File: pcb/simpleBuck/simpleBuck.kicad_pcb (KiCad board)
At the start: 4 copper layers, 76.2 x 50.8 mm, 65 parts, among them J1 Conn_01x04, J2 Conn_01x06, J3 Conn_01x04, J4 Conn_01x02, J5 Conn_01x02, J6 Conn_01x02, Q1 TRANSISTOR_PNPMMBT4403, U1 TI_INA181A2, U2 TI_TL072HIDBVR, U3 TI_TL072HIDBVR, U4 NATIONALSEMI_LM2596SX-ADJ, U5 ANALOG_MAX539BCSA+, U6 ANALOG_MAX539BCSA+

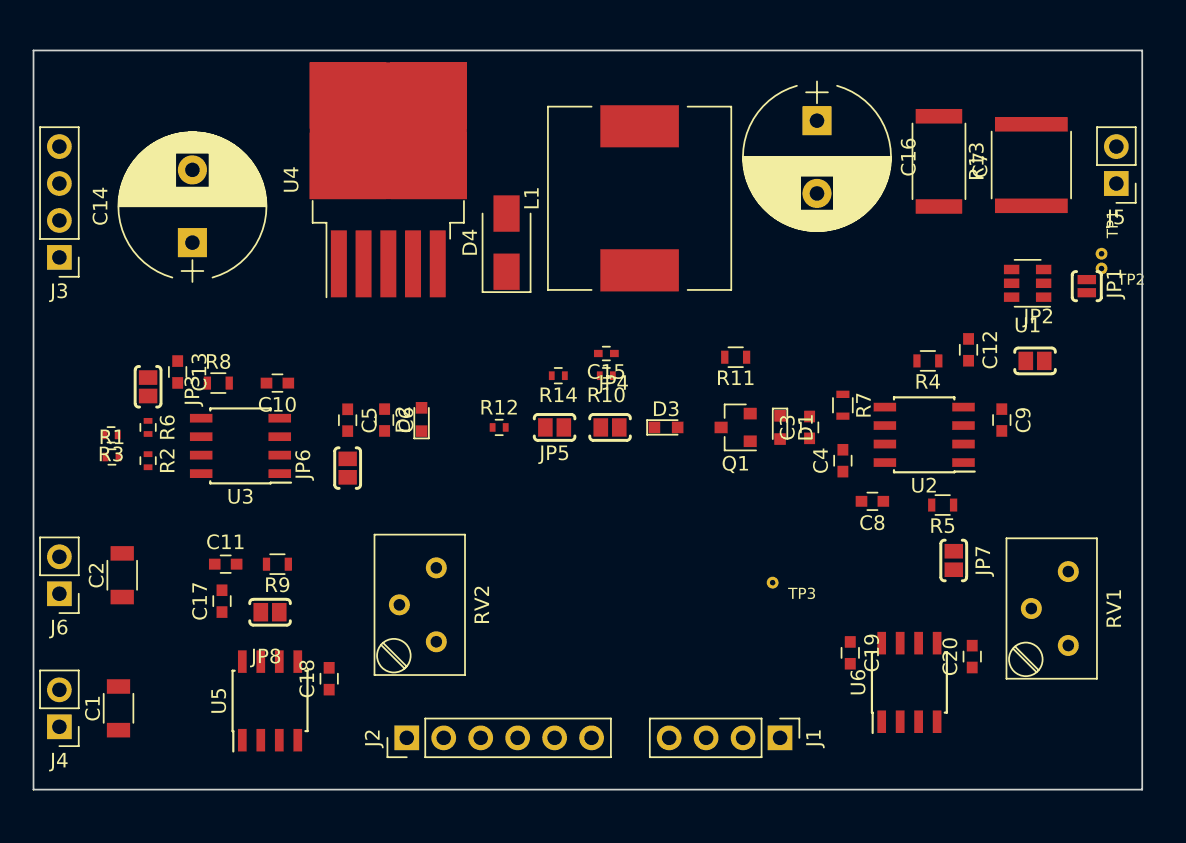
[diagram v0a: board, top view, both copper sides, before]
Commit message: Updated schematic to include lm2596 on board.
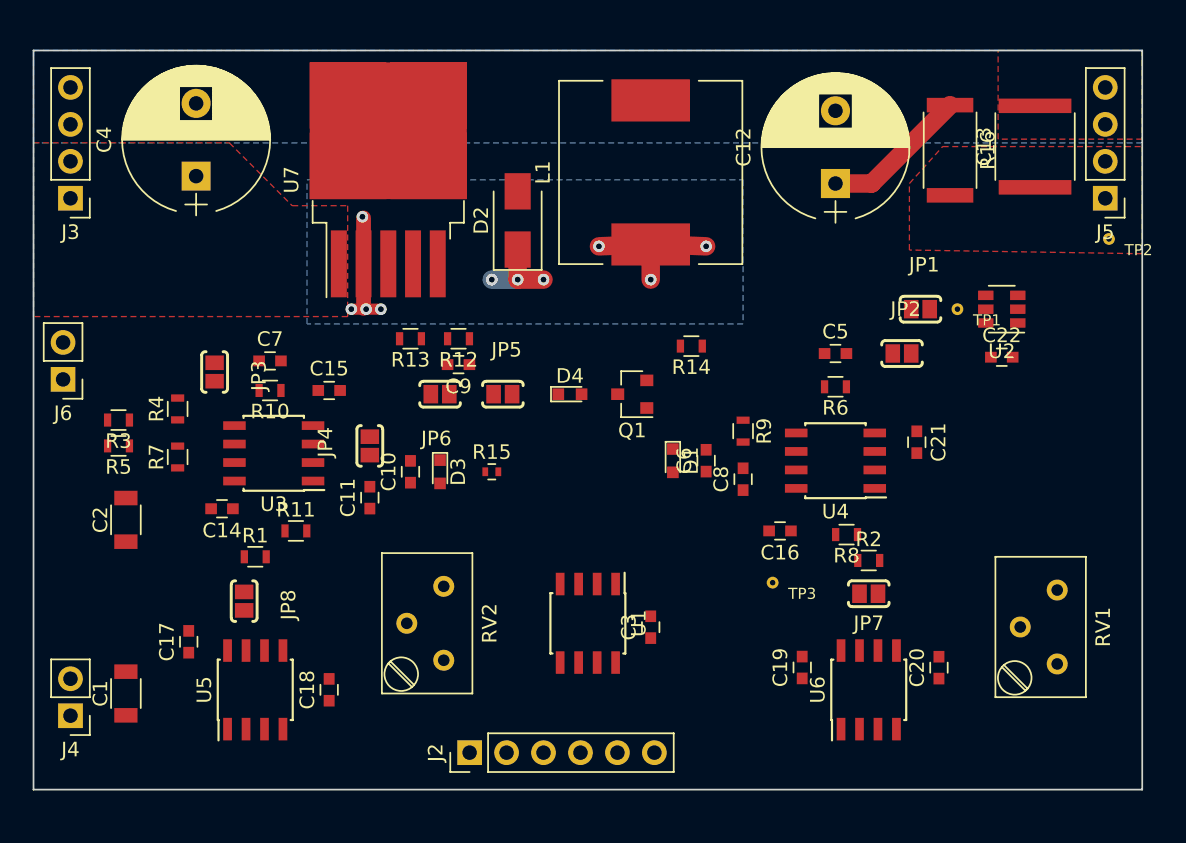
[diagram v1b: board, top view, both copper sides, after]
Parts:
- removed J1: Conn_01x04, Pin_Headers:Pin_Header_Straight_1x04_Pitch2.54mm
- added C21: MURATA_GCJ188R91H104KA01D, Capacitors_SMD:C_0603, F.Cu at (975.1, 204.7)
- added C22: MURATA_GCJ188R91H104KA01D, Capacitors_SMD:C_0603, F.Cu at (980.9, 198.9)
- added R15: VISHAYDALE_CRCW0402150KFKEDC, Resistors_SMD:R_0402, F.Cu at (945.9, 206.8)
- added R16: STACKPOLE_CSRT2512FT50L0-UP, Resistors_SMD:R_2512, F.Cu at (977.4, 184.7)
- added U7: NATIONALSEMI_LM2596SX-ADJ, TO_SOT_Packages_SMD:TO-263-5_TabPin6, F.Cu at (938.8, 186.7)
- C10, C11, C8, C9: value MURATA_GCJ188R91H104KA01D -> KEMET_C0603C103K5RAL7867
- C12: value KEMET_C0603C103K5RAL7867 -> PANASONIC_EEU-FC1H221B; footprint Capacitors_SMD:C_0603 -> Capacitors_THT:CP_Radial_D10.0mm_P5.00mm
- C13: value KEMET_C0603C103K5RAL7867 -> MURATA_KRM55WR7YA476MH01L; footprint Capacitors_SMD:C_0603 -> Capacitors_SMD:C_2220
- C14: value RUBYCON_100ZLH100MEFC10X20 -> MURATA_GCJ188R91H104KA01D; footprint Capacitors_THT:CP_Radial_D10.0mm_P5.00mm -> Capacitors_SMD:C_0603
- C15: value MURATA_GCM155R71E103KA37D -> MURATA_GCJ188R91H104KA01D; footprint Capacitors_SMD:C_0402 -> Capacitors_SMD:C_0603
- C16: value PANASONIC_EEU-FC1H221B -> MURATA_GCJ188R91H104KA01D; footprint Capacitors_THT:CP_Radial_D10.0mm_P5.00mm -> Capacitors_SMD:C_0603
- C3: value KEMET_C0603C103K5RAL7867 -> MURATA_GCJ188R91H104KA01D
- C4: value KEMET_C0603C103K5RAL7867 -> RUBYCON_100ZLH100MEFC10X20; footprint Capacitors_SMD:C_0603 -> Capacitors_THT:CP_Radial_D10.0mm_P5.00mm
- C7: value MURATA_KRM55WR7YA476MH01L -> KEMET_C0603C103K5RAL7867; footprint Capacitors_SMD:C_2220 -> Capacitors_SMD:C_0603
- D2: value MICRO_COMMERCIAL_1N4148X-TP -> VISHAY_SSA34HE3_A_I; footprint LEDs:LED_0603 -> Diodes_SMD:D_SMA
- D4: value VISHAY_SSA34HE3_A_I -> MICRO_COMMERCIAL_1N4148X-TP; footprint Diodes_SMD:D_SMA -> LEDs:LED_0603
- J5: value Conn_01x02 -> Conn_01x04; footprint Pin_Headers:Pin_Header_Straight_1x02_Pitch2.54mm -> Pin_Headers:Pin_Header_Straight_1x04_Pitch2.54mm
- R1, R10, R2, R6: value VISHAYDALE_CRCW04021M00FKEDC -> VISHAY_CRCW060310K0FKEBC; footprint Resistors_SMD:R_0402 -> Resistors_SMD:R_0603
- R11: value SMD-RES-1.0K-0603 -> VISHAY_CRCW060310K0FKEBC
- R12: value VISHAYDALE_CRCW0402150KFKEDC -> VISHAYDALE_CRCW06031M00FKEAC; footprint Resistors_SMD:R_0402 -> Resistors_SMD:R_0603
- R13: value STACKPOLE_CSRT2512FT50L0-UP -> VISHAYDALE_CRCW060368K0FKEA; footprint Resistors_SMD:R_2512 -> Resistors_SMD:R_0603
- R14: value VISHAYDALE_CRCW040268K0FKEDC -> SMD-RES-1.0K-0603; footprint Resistors_SMD:R_0402 -> Resistors_SMD:R_0603
- R3: value VISHAYDALE_CRCW04021M00FKEDC -> VISHAYDALE_CRCW06031M00FKEAC; footprint Resistors_SMD:R_0402 -> Resistors_SMD:R_0603
- R4, R5, R7: value VISHAY_CRCW060310K0FKEBC -> VISHAYDALE_CRCW06031M00FKEAC
- U1: value TI_INA181A2 -> ANALOG_LTC1288CS8#PBF; footprint TO_SOT_Packages_SMD:SOT-23-6 -> Housings_SOIC:SOIC-8_3.9x4.9mm_Pitch1.27mm
- U2: value TI_TL072HIDBVR -> TI_INA181A2; footprint Housings_SOIC:SOIC-8_3.9x4.9mm_Pitch1.27mm -> TO_SOT_Packages_SMD:SOT-23-6
- U4: value NATIONALSEMI_LM2596SX-ADJ -> TI_TL072HIDBVR; footprint TO_SOT_Packages_SMD:TO-263-5_TabPin6 -> Housings_SOIC:SOIC-8_3.9x4.9mm_Pitch1.27mm
- moved C13 60.9 mm to (983.2, 184.4), turned to 90 degrees
- moved R5 56.8 mm to (920.2, 205.0)
- moved C7 54.0 mm to (930.7, 199.1), turned to 0 degrees
- moved R4 51.7 mm to (924.3, 202.4), turned to 90 degrees
- moved R2 50.0 mm to (971.8, 212.9), turned to 0 degrees
- moved C4 48.6 mm to (925.6, 186.4)
- moved R6 47.3 mm to (969.5, 200.9), turned to 180 degrees
- moved R7 45.9 mm to (924.3, 205.7), turned to 90 degrees
- moved R8 44.4 mm to (970.3, 211.1), turned to 180 degrees
- moved R13 38.3 mm to (940.3, 197.6), turned to 180 degrees
- moved U1 38.2 mm to (952.5, 217.2), turned to 270 degrees
- moved C9 37.5 mm to (943.6, 199.4), turned to 180 degrees
- moved U4 36.3 mm to (969.5, 206.0), turned to 180 degrees
- moved C5 33.8 mm to (969.5, 198.6), turned to 0 degrees
- moved R9 33.3 mm to (963.2, 204.0), turned to 270 degrees
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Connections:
- C10 pad 1: +5VA -> Net-(C10-Pad1)
- C10 pad 2: GND -> Net-(C10-Pad2)
- C11 pad 1: -5VA -> Net-(C10-Pad1)
- C11 pad 2: GND -> Net-(C11-Pad2)
- C12 pad 1: GND -> /power_stage/VOUT_HI
- C12 pad 2: /I_ADC -> GND
- C13 pad 1: GND -> /VOUT
- C13 pad 2: /V_ADC -> GND
- C14 pad 1: VIN -> +5VA
- C15 pad 1: /VOUT_HI -> -5VA
- C15 pad 2: /V_FB -> GND
- C16 pad 1: /VOUT_HI -> +5VA
- C17 pad 1: VDD -> +5VA
- C18 pad 1: +5VA -> VREF
- C19 pad 1: VDD -> +5VA
- C20 pad 1: +5VA -> VREF
- C3 pad 1: Net-(C3-Pad1) -> VREF
- C3 pad 2: Net-(C3-Pad2) -> GND
- C4 pad 1: Net-(C3-Pad1) -> VIN
- C4 pad 2: Net-(C4-Pad2) -> GND
- C5 pad 1: Net-(C5-Pad1) -> GND
- C5 pad 2: Net-(C5-Pad2) -> /I_ADC
- C6 pad 1: Net-(C5-Pad1) -> Net-(C6-Pad1)
- C7 pad 1: /VOUT -> GND
- C7 pad 2: GND -> /V_ADC
- C8 pad 1: +5VA -> Net-(C6-Pad1)
- C8 pad 2: GND -> Net-(C8-Pad2)
- C9 pad 1: -5VA -> /power_stage/VOUT_HI
- C9 pad 2: GND -> /power_stage/V_FB
- D1 pad 1: Net-(C3-Pad2) -> Net-(C6-Pad2)
- D1 pad 2: Net-(C3-Pad1) -> Net-(C6-Pad1)
- D2 pad 1: Net-(C5-Pad2) -> Net-(D2-Pad1)
- D2 pad 2: Net-(C5-Pad1) -> GND
- D3 pad 1: Net-(D3-Pad1) -> Net-(C10-Pad2)
- D3 pad 2: Net-(D3-Pad2) -> Net-(C10-Pad1)
- D4 pad 2: GND -> Net-(D4-Pad2)
- J2 pad 1: VDD -> +5VA
- J2 pad 5: /SYNC -> /CS_VSET
- J5 pad 2: GND -> /VOUT
- JP4 pad 1: Net-(D3-Pad1) -> Net-(C10-Pad2)
- JP4 pad 2: /V_FB -> Net-(C11-Pad2)
- JP5 pad 1: Net-(JP5-Pad1) -> Net-(D4-Pad1)
- JP5 pad 2: /V_FB -> /power_stage/V_FB
- JP6 pad 1: Net-(C5-Pad2) -> Net-(JP6-Pad1)
- JP6 pad 2: Net-(C6-Pad2) -> /power_stage/V_FB
- L1 pad 1: Net-(D4-Pad1) -> Net-(D2-Pad1)
- L1 pad 2: /VOUT_HI -> /power_stage/VOUT_HI
- Q1 pad 1: Net-(C3-Pad1) -> Net-(C6-Pad1)
- Q1 pad 3: Net-(D3-Pad2) -> Net-(D4-Pad2)
- R1 pad 1: /VOUT -> /V_SET
- R1 pad 2: Net-(R1-Pad2) -> GND
- R10 pad 1: /VOUT_HI -> /V_ADC
- R10 pad 2: /V_FB -> Net-(C10-Pad2)
- R11 pad 1: /VOUT -> /V_SET
- R11 pad 2: Net-(Q1-Pad2) -> Net-(R11-Pad2)
- R12 pad 1: Net-(C5-Pad1) -> /power_stage/VOUT_HI
- R12 pad 2: Net-(JP5-Pad1) -> /power_stage/V_FB
- R13 pad 1: /VOUT_HI -> /power_stage/V_FB
- R13 pad 2: /VOUT -> GND
- R14 pad 1: /V_FB -> /VOUT
- R14 pad 2: GND -> Net-(Q1-Pad2)
- R2 pad 1: Net-(R1-Pad2) -> /I_SET
- R3 pad 2: GND -> /VOUT
- R4 pad 1: /I_ADC -> Net-(R3-Pad1)
- R4 pad 2: Net-(C3-Pad2) -> GND
- R5 pad 1: /I_SET -> Net-(R5-Pad1)
- R5 pad 2: Net-(R5-Pad2) -> GND
- R6 pad 1: Net-(JP3-Pad1) -> /I_ADC
- R6 pad 2: Net-(R3-Pad1) -> Net-(C6-Pad2)
- R7 pad 1: Net-(C3-Pad2) -> Net-(JP3-Pad1)
- R7 pad 2: Net-(C4-Pad2) -> Net-(R5-Pad1)
- R8 pad 1: /V_ADC -> /I_SET
- R8 pad 2: Net-(C5-Pad2) -> Net-(R8-Pad2)
- R9 pad 1: /V_SET -> Net-(C6-Pad2)
- R9 pad 2: Net-(R9-Pad2) -> Net-(C8-Pad2)
- U1 pad 1: Net-(JP2-Pad1) -> /CS_ISET
- U1 pad 2: GND -> /I_ADC
- U1 pad 3: /VOUT_HI -> /V_ADC
- U1 pad 4: /VOUT -> GND
- U1 pad 5: Net-(JP1-Pad1) -> /SDIN
- U1 pad 6: +5VA -> Net-(U1-Pad6)
- U2 pad 1: (no net) -> Net-(JP2-Pad1)
- U2 pad 2: (no net) -> GND
- U2 pad 3: (no net) -> /power_stage/VOUT_HI
- U2 pad 4: -5VA -> /VOUT
- U2 pad 5: Net-(C3-Pad2) -> Net-(JP1-Pad1)
- U2 pad 6: Net-(R5-Pad2) -> +5VA
- U3 pad 1: Net-(C5-Pad1) -> Net-(C10-Pad1)
- U3 pad 2: Net-(R9-Pad2) -> Net-(R11-Pad2)
- U3 pad 3: Net-(C5-Pad2) -> Net-(C10-Pad2)
- U3 pad 5: Net-(R1-Pad2) -> Net-(R3-Pad1)
- U3 pad 6: Net-(R3-Pad1) -> Net-(R5-Pad1)
- U4 pad 1: VIN -> (no net)
- U4 pad 2: Net-(D4-Pad1) -> (no net)
- U4 pad 3: GND -> (no net)
- U4 pad 4: /V_FB -> -5VA
- U4 pad 5: /ENABLE -> Net-(C6-Pad2)
- U4 pad 6: GND -> Net-(R8-Pad2)
- U5 pad 3: /SYNC -> /CS_VSET
- U5 pad 6: +5VA -> VREF
- U5 pad 8: VDD -> +5VA
- U6 pad 1: Net-(U5-Pad4) -> /SDIN
- U6 pad 3: /SYNC -> /CS_ISET
- U6 pad 6: +5VA -> VREF
- U6 pad 8: VDD -> +5VA
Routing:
- net Net-(D2-Pad1): track 0.00 -> 24.0 mm, vias 0 -> 10
- net /power_stage/VOUT_HI: track 0.00 -> 10.1 mm
- added copper zone on F.Cu, net /VOUT
- added copper zone on B.Cu, net GND
- added copper zone on F.Cu, net GND
- added copper zone on B.Cu, net Net-(D2-Pad1)
- added copper zone on F.Cu, net VIN

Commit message: Added jumpers and finalized DAC/ADC selection.
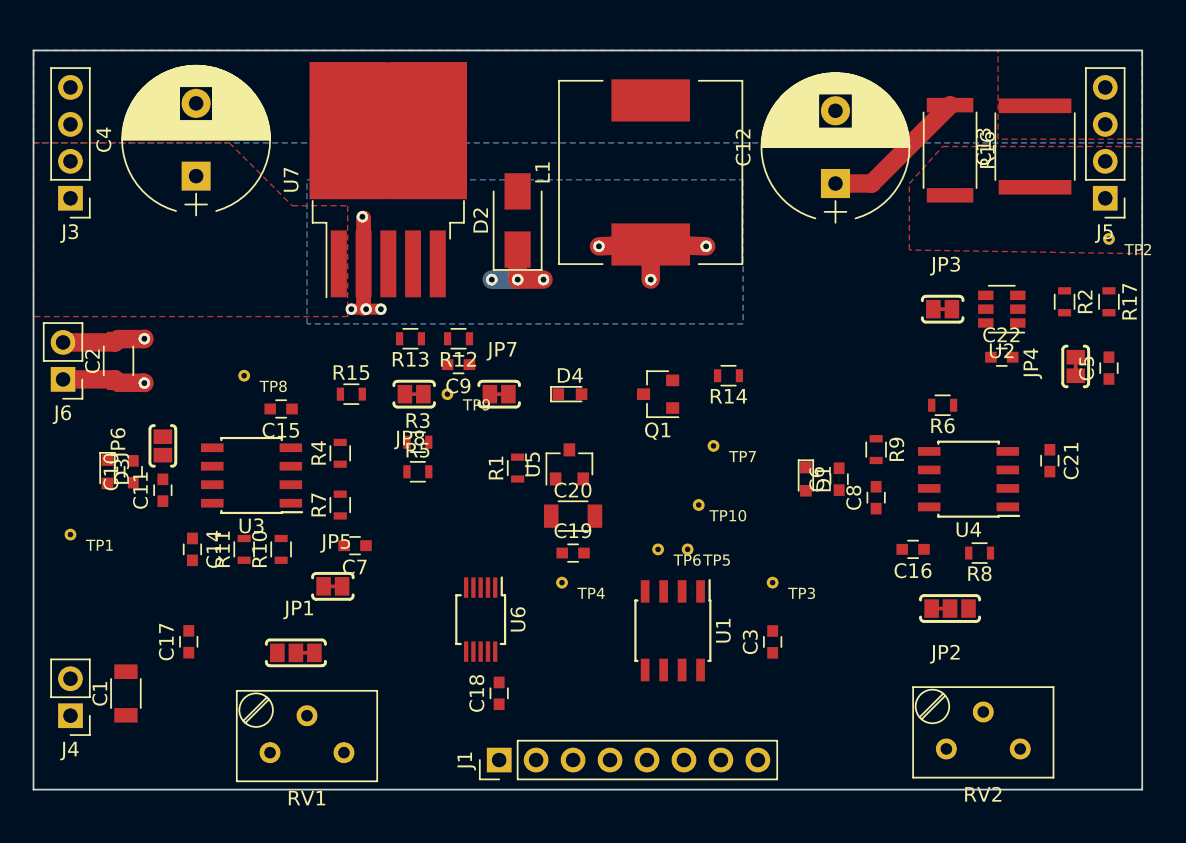
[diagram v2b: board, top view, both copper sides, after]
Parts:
- removed J2: Conn_01x06, Pin_Headers:Pin_Header_Straight_1x06_Pitch2.54mm
- added J1: Conn_01x08, Pin_Headers:Pin_Header_Straight_1x08_Pitch2.54mm, F.Cu at (946.4, 226.6)
- added R17: VISHAY_CRCW060310K0FKEBC, Resistors_SMD:R_0603, F.Cu at (988.3, 195.1)
- added TP10: DBLS_TESTPOINT_NORMAL, DBLS_Misc:DBLS_Testpoint_Normal, F.Cu at (960.1, 209.0)
- added TP4: DBLS_TESTPOINT_NORMAL, DBLS_Misc:DBLS_Testpoint_Normal, F.Cu at (950.7, 214.4)
- added TP5: DBLS_TESTPOINT_NORMAL, DBLS_Misc:DBLS_Testpoint_Normal, F.Cu at (959.4, 212.1)
- added TP6: DBLS_TESTPOINT_NORMAL, DBLS_Misc:DBLS_Testpoint_Normal, F.Cu at (957.3, 212.1)
- added TP7: DBLS_TESTPOINT_NORMAL, DBLS_Misc:DBLS_Testpoint_Normal, F.Cu at (961.1, 205.0)
- added TP8: DBLS_TESTPOINT_NORMAL, DBLS_Misc:DBLS_Testpoint_Normal, F.Cu at (928.9, 200.2)
- added TP9: DBLS_TESTPOINT_NORMAL, DBLS_Misc:DBLS_Testpoint_Normal, F.Cu at (942.8, 201.4)
- C20: value MURATA_GCJ188R91H104KA01D -> MURATA_GRT31CR61H106KE01L; footprint Capacitors_SMD:C_0603 -> Capacitors_SMD:C_1206
- JP1: value PAD_JUMPER_2PIN_NC -> PAD_JUMPER_3PIN_12_NC_BY_TRACE; footprint DBLS_Misc:PAD_JUMPER_2PIN_NC -> DBLS_Jumpers:PAD_JUMPER_3PIN_12_NC_BY_TRACE
- JP2: value PAD_JUMPER_2PIN_0603 -> PAD_JUMPER_3PIN_12_NC_BY_TRACE; footprint DBLS_Misc:PAD_JUMPER_2PIN_0603 -> DBLS_Jumpers:PAD_JUMPER_3PIN_12_NC_BY_TRACE
- JP3, JP4, JP5, JP7, JP8: value PAD_JUMPER_2PIN_0603 -> PAD_JUMPER_2PIN_NC_BY_TRACE; footprint DBLS_Misc:PAD_JUMPER_2PIN_0603 -> DBLS_Jumpers:PAD_JUMPER_2PIN_NC_BY_TRACE
- JP6: value PAD_JUMPER_2PIN_0603 -> PAD_JUMPER_2PIN_NO; footprint DBLS_Misc:PAD_JUMPER_2PIN_0603 -> DBLS_Jumpers:PAD_JUMPER_2PIN_NO_0603
- R1: value VISHAY_CRCW060310K0FKEBC -> VISHAYDALE_CRCW0603604RFKEAHP
- R15: value VISHAYDALE_CRCW0402150KFKEDC -> VISHAYDALE_CRCW0603150KFKEAC; footprint Resistors_SMD:R_0402 -> Resistors_SMD:R_0603
- U5: value ANALOG_MAX539BCSA+ -> TI_LM4040C41IDBZT; footprint Housings_SOIC:SOIC-8_3.9x4.9mm_Pitch1.27mm -> TO_SOT_Packages_SMD:SOT-23
- U6: value ANALOG_MAX539BCSA+ -> TI_DAC122S085CIMM_NOPB; footprint Housings_SOIC:SOIC-8_3.9x4.9mm_Pitch1.27mm -> Housings_SSOP:MSOP-10_3x3mm_Pitch0.5mm
- moved TP1 62.9 mm to (916.9, 211.1)
- moved RV1 54.4 mm to (930.7, 226.1), turned to 180 degrees
- moved JP3 50.2 mm to (976.9, 195.6), turned to 180 degrees
- moved JP1 49.0 mm to (932.4, 219.2)
- moved JP4 48.8 mm to (986.0, 199.5)
- moved RV2 35.1 mm to (977.1, 225.8), turned to 180 degrees
- moved JP7 28.9 mm to (946.4, 201.4), turned to 180 degrees
- moved C20 27.2 mm to (951.5, 209.8), turned to 0 degrees
- moved U6 27.1 mm to (945.1, 216.9), turned to 270 degrees
- moved U5 26.6 mm to (951.2, 206.2)
- moved D3 22.9 mm to (919.5, 206.8)
- moved R2 22.3 mm to (985.3, 195.1), turned to 270 degrees
- moved R5 20.7 mm to (940.8, 206.8), turned to 0 degrees
- moved R3 20.6 mm to (940.8, 204.7), turned to 0 degrees
- moved JP6 19.4 mm to (923.3, 205.0), turned to 270 degrees
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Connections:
- C19 pad 1: +5VA -> VREF
- JP1 pad 2: GND -> /V_SET
- JP2 pad 2: /I_ADC -> /I_SET
- JP3 pad 2: /V_ADC -> GND
- JP4 pad 1: Net-(C10-Pad2) -> /I_ADC
- JP4 pad 2: Net-(C11-Pad2) -> Net-(JP4-Pad2)
- JP5 pad 1: Net-(D4-Pad1) -> /V_ADC
- JP5 pad 2: /power_stage/V_FB -> Net-(JP5-Pad2)
- JP6 pad 1: Net-(JP6-Pad1) -> Net-(C10-Pad2)
- JP6 pad 2: /power_stage/V_FB -> Net-(C11-Pad2)
- JP7 pad 1: Net-(JP7-Pad1) -> Net-(D4-Pad1)
- JP7 pad 2: /I_SET -> /power_stage/V_FB
- JP8 pad 2: /V_SET -> /power_stage/V_FB
- R1 pad 1: /V_SET -> VREF
- R1 pad 2: GND -> +5VA
- R10 pad 1: /V_ADC -> Net-(JP5-Pad2)
- R15 pad 2: Net-(JP6-Pad1) -> Net-(JP8-Pad1)
- R2 pad 1: /I_SET -> /power_stage/VOUT_HI
- R6 pad 1: /I_ADC -> Net-(JP4-Pad2)
- R7 pad 1: Net-(JP3-Pad1) -> /V_ADC
- RV1 pad 2: /I_SET -> /V_POT
- RV2 pad 2: /V_SET -> /I_POT
- TP1 pad 1: Net-(JP1-Pad1) -> GND
- U1 pad 1: /CS_ISET -> /CS_ADC
- U1 pad 6: Net-(U1-Pad6) -> /ADC_DOUT
- U2 pad 1: Net-(JP2-Pad1) -> /I_ADC
- U2 pad 5: Net-(JP1-Pad1) -> Net-(JP3-Pad1)
- U3 pad 1: Net-(C10-Pad1) -> /V_ADC
- U3 pad 2: Net-(R11-Pad2) -> Net-(R5-Pad1)
- U3 pad 3: Net-(C10-Pad2) -> Net-(R3-Pad1)
- U3 pad 5: Net-(R3-Pad1) -> Net-(C10-Pad2)
- U3 pad 6: Net-(R5-Pad1) -> Net-(R11-Pad2)
- U3 pad 7: Net-(JP3-Pad1) -> Net-(C10-Pad1)
- U5 pad 1: /SDIN -> VREF
- U5 pad 2: /SCLK -> GND
- U5 pad 3: /CS_VSET -> (no net)
- U6 pad 1: /SDIN -> +5VA
- U6 pad 2: /SCLK -> Net-(JP1-Pad1)
- U6 pad 3: /CS_ISET -> Net-(JP2-Pad1)
- U6 pad 5: GND -> Net-(U6-Pad5)
- U6 pad 6: VREF -> GND
- U6 pad 7: Net-(JP7-Pad1) -> VREF
- U6 pad 8: +5VA -> /SDIN
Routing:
- net GND: track 0.00 -> 5.69 mm, vias 0 -> 1
- net -5VA: track 0.00 -> 5.69 mm, vias 0 -> 1

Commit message: Prelim Layout before silkscreen tuning.
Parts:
- removed TP10: DBLS_TESTPOINT_NORMAL, DBLS_Misc:DBLS_Testpoint_Normal
- moved TP2 48.3 mm to (942.6, 206.2)
- moved C17 22.8 mm to (946.9, 211.8), turned to 0 degrees
- moved C5 21.5 mm to (967.0, 197.4), turned to 0 degrees
- moved R17 20.3 mm to (976.1, 178.8), turned to 180 degrees
- moved R2 17.5 mm to (978.9, 178.8), turned to 0 degrees
- moved C3 11.0 mm to (954.3, 216.9)
- moved U2 9.91 mm to (971.0, 195.6), turned to 0 degrees
- moved C22 9.01 mm to (974.1, 193.0), turned to 90 degrees
- moved C18 5.67 mm to (948.9, 216.9)
- moved JP4 5.17 mm to (981.5, 201.9)
- moved R14 3.57 mm to (958.6, 200.2)
- moved D2 3.56 mm to (947.7, 185.9)
- moved TP4 3.30 mm to (950.7, 217.7)
- moved TP7 2.59 mm to (960.6, 202.4)
- moved Q1 2.54 mm to (954.8, 201.4)
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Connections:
- J1 pad 3: /SCLK -> /SDIN
- J1 pad 4: /SDIN -> /ADC_DOUT
- J1 pad 5: /ADC_DOUT -> /SCLK
- J1 pad 6: /CS_ADC -> /CS_DAC
- J1 pad 7: /CS_DAC -> /CS_ADC
- U6 pad 2: Net-(JP1-Pad1) -> Net-(JP2-Pad1)
- U6 pad 3: Net-(JP2-Pad1) -> Net-(JP1-Pad1)
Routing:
- net GND: track 5.69 -> 97.3 mm, vias 1 -> 49
- net /VOUT: track 0.00 -> 72.1 mm, vias 0 -> 1
- net /power_stage/VOUT_HI: track 10.1 -> 61.6 mm
- net +5VA: track 0.00 -> 47.2 mm, vias 0 -> 6
- net /ENABLE: track 0.00 -> 46.3 mm, vias 0 -> 1
- net /I_ADC: track 0.00 -> 40.2 mm, vias 0 -> 1
- net /V_ADC: track 0.00 -> 36.3 mm, vias 0 -> 1
- net Net-(JP2-Pad1): track 0.00 -> 34.6 mm, vias 0 -> 2
- net VREF: track 0.00 -> 34.3 mm
- net Net-(C10-Pad1): track 0.00 -> 30.5 mm
- net Net-(C6-Pad1): track 0.00 -> 23.8 mm
- net /SDIN: track 0.00 -> 22.2 mm
- net /SCLK: track 0.00 -> 21.2 mm
- net /CS_ADC: track 0.00 -> 18.3 mm, vias 0 -> 1
- net Net-(C10-Pad2): track 0.00 -> 17.7 mm
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- added copper zone on In2.Cu, net +5VA
- added copper zone on In2.Cu, net -5VA
- added copper zone on F.Cu, net /power_stage/VOUT_HI
- added copper zone on In1.Cu, net GND
- added copper zone on In2.Cu, net GND
- added copper zone on F.Cu, net Net-(D2-Pad1)
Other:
- net class Default: clearance 0.2 -> 0.2032; trace_width 0.25 -> 0.254; via_dia 0.8 -> 0.8128; via_drill 0.4 -> 0.381
- rule trace_clearance: 0.2 -> 0.2032
- rule trace_min: 0.2 -> 0.254
- rule via_min_drill: 0.3 -> 0.3048
- rule via_min_size: 0.4 -> 0.762

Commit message: Finished layout. Heading to fab
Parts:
- added LOGO1: DBLS_Chicken_Small, DBLS_LOGO:Rooster_4mmx4mm, F.Cu at (928.9, 193.0)
- added LOGO2: DBLS_van_logo_small_v1, DBLS_LOGO:van_logo_small, B.Cu at (940.6, 208.3)
- added LOGO3: DBLS_van_logo_8mmX6mm, DBLS_LOGO:van_logo_8mmX6mm, F.Cu at (971.3, 218.4)
- moved C14 1.44 mm to (925.6, 212.6)
- moved J1 1.14 mm to (947.4, 226.1)
- moved JP7 0.76 mm to (945.9, 201.4)
- moved RV2 0.25 mm to (977.1, 226.1)
- moved TP2 0.25 mm to (942.6, 206.0)
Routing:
- net /CS_ADC: track 18.3 -> 12.1 mm, vias 1 -> 0
- net /ADC_DOUT: track 8.61 -> 6.79 mm
- net /ENABLE: track 46.3 -> 47.9 mm
- net /power_stage/V_FB: track 17.4 -> 18.5 mm
- net /SDIN: track 22.2 -> 21.1 mm
- net /SCLK: track 21.2 -> 20.2 mm
- net /CS_DAC: track 17.2 -> 18.0 mm
- net Net-(D4-Pad1): track 3.39 -> 2.63 mm
- net +5VA: track 47.2 -> 47.7 mm
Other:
- board text added: "-5VA"
- board text added: "5VA"
- board text added: "ADC"
- board text added: "CLK"
- board text added: "DAC"
- board text added: "DIN"
- board text added: "DIRTBAG LAB SUPPLIES"
- board text added: "DOUT"
- board text added: "Dirtbag Lab Supplies SimpleBuck rev1.0 04/2022"
- board text added: "EN"
- board text added: "GND"
- board text added: "I_ADC"
- board text added: "I_DRIVE"
- board text added: "I_SET"
- board text added: "VIN"
- board text added: "VOUT"
- board text added: "VREF"
- board text added: "V_ADC"
- board text added: "V_DRIVE"
- board text added: "V_SET"
